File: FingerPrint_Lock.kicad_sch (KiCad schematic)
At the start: 11 parts, among them J1 Fingerprint Sensor, J2 12V Solenoid Lock, J3 12V Relay, SW1 Button1, SW2 Button2, SW3 Button3, U2 I2C 2X16 LCD

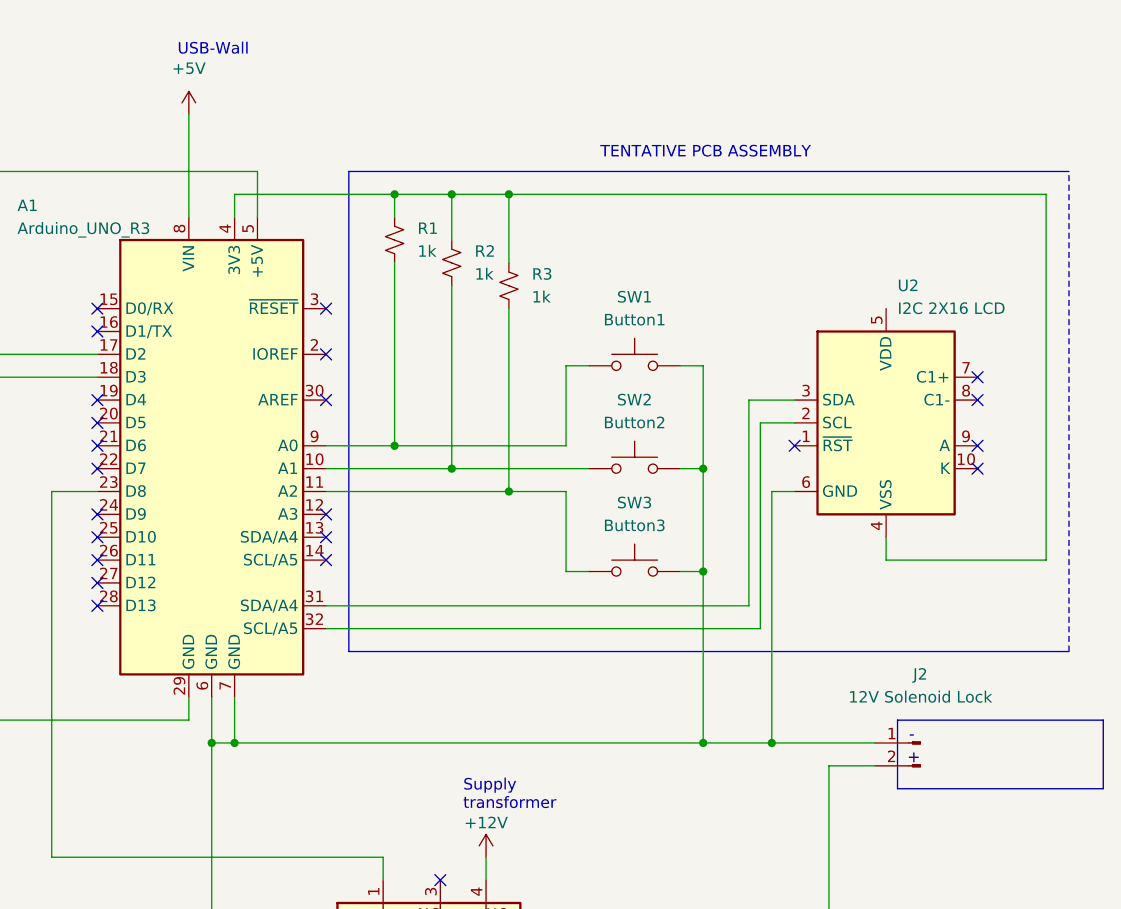
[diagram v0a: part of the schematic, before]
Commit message: Add files via upload
Corrected connections and labels. Added 4th button.
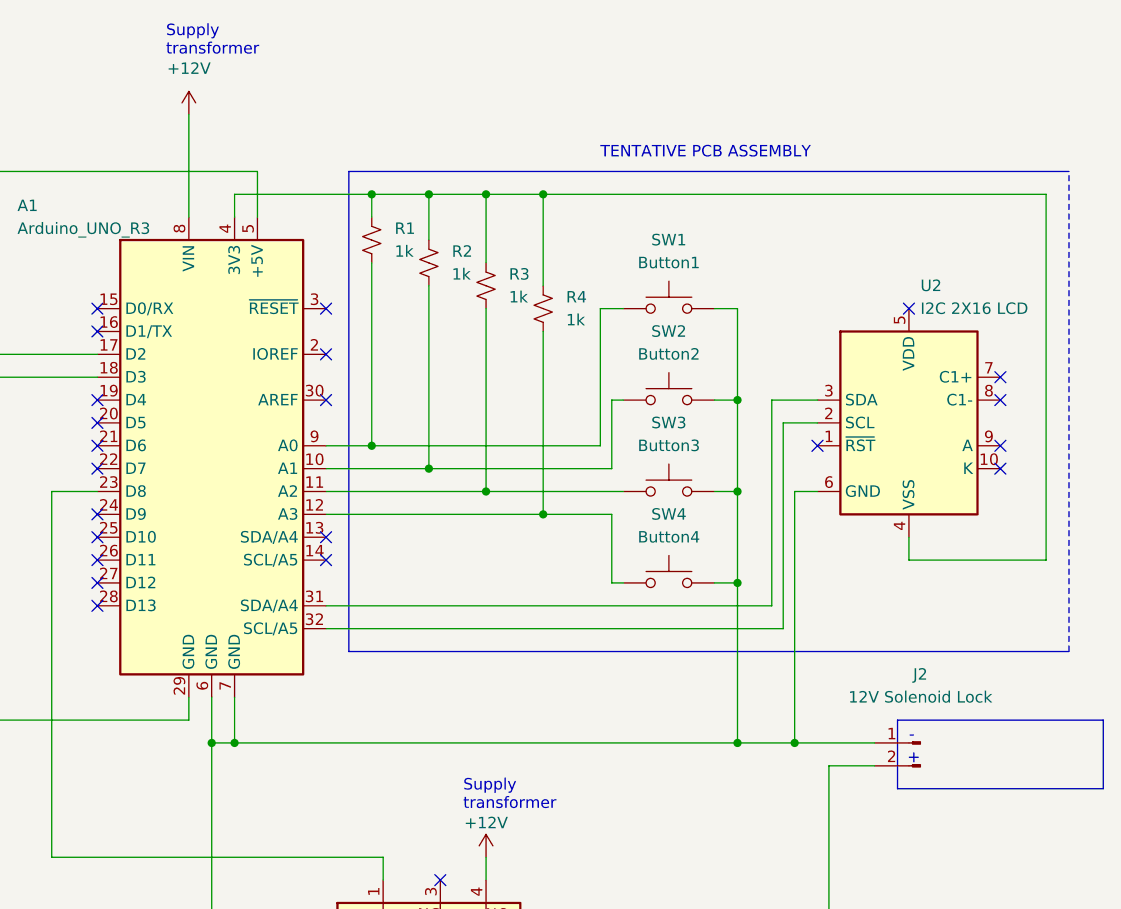
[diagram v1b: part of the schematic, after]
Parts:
- added R4: 1k, symbol Device:R_Small_US
- added SW4: Button4, symbol Switch:SW_Push
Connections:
- net +5V is gone; now on net +12V: A1.8 (VIN)
- net at A1.4 (3V3), R1.1, R2.1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: now also R4.1
- net at A1.6 (GND), A1.7 (GND), J2.1 (Pin_1)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: now also SW4.2
- net at A1.12 (A3): now also R4.2, SW4.1
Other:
- note removed: "USB-Wall"
- moved on the sheet: R1, R2, R3, SW1, SW2, SW3, U2

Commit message: Final(?) schematics/PCB upload
Final(?) version of overview schematic, PCB file, and PCB Schematic.
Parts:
- added R5: 100R, symbol Device:R_US
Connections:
- net +12V: now also J3.1, J3.6; no longer J3.4
- net at A1.4 (3V3), R1.1, R2.1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: now also J1.1 (Pin_1); no longer U2.4 (VSS)
- net at R2.2, SW2.1: now also A1.20 (D5); no longer A1.10 (A1)
- net at A1.5 (+5V): now also U2.2 (VCC); no longer J1.1 (Pin_1)
- net at A1.29 (GND), J1.4 (Pin_4): now also A1.6 (GND), A1.7 (GND), J2.1 (Pin_1), J3.2, SW1.2, SW2.2, SW3.2, SW4.2, U2.1 (GND)
- net at A1.23 (D8): now also R5.1; no longer J3.1
- net at J3.3: now also R5.2
- net at R1.2, SW1.1: now also A1.19 (D4); no longer A1.9 (A0)
- net at R4.2, SW4.1: now also A1.22 (D7); no longer A1.12 (A3)
- net at R3.2, SW3.1: now also A1.21 (D6); no longer A1.11 (A2)
- net at A1.32 (SCL/A5): now also U2.4 (SCL); no longer U2.2 (SCL)
- no-connect marks 24 -> 17
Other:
- note added: "3V3"
- note added: "PCB ASSEMBLY"
- note removed: "5V"
- note removed: "TENTATIVE PCB ASSEMBLY"
- moved on the sheet: A1, J1, J2, J3, R1, R2, R3, R4, SW1, SW2, SW3, SW4
